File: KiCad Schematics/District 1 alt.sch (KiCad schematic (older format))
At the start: 23 parts

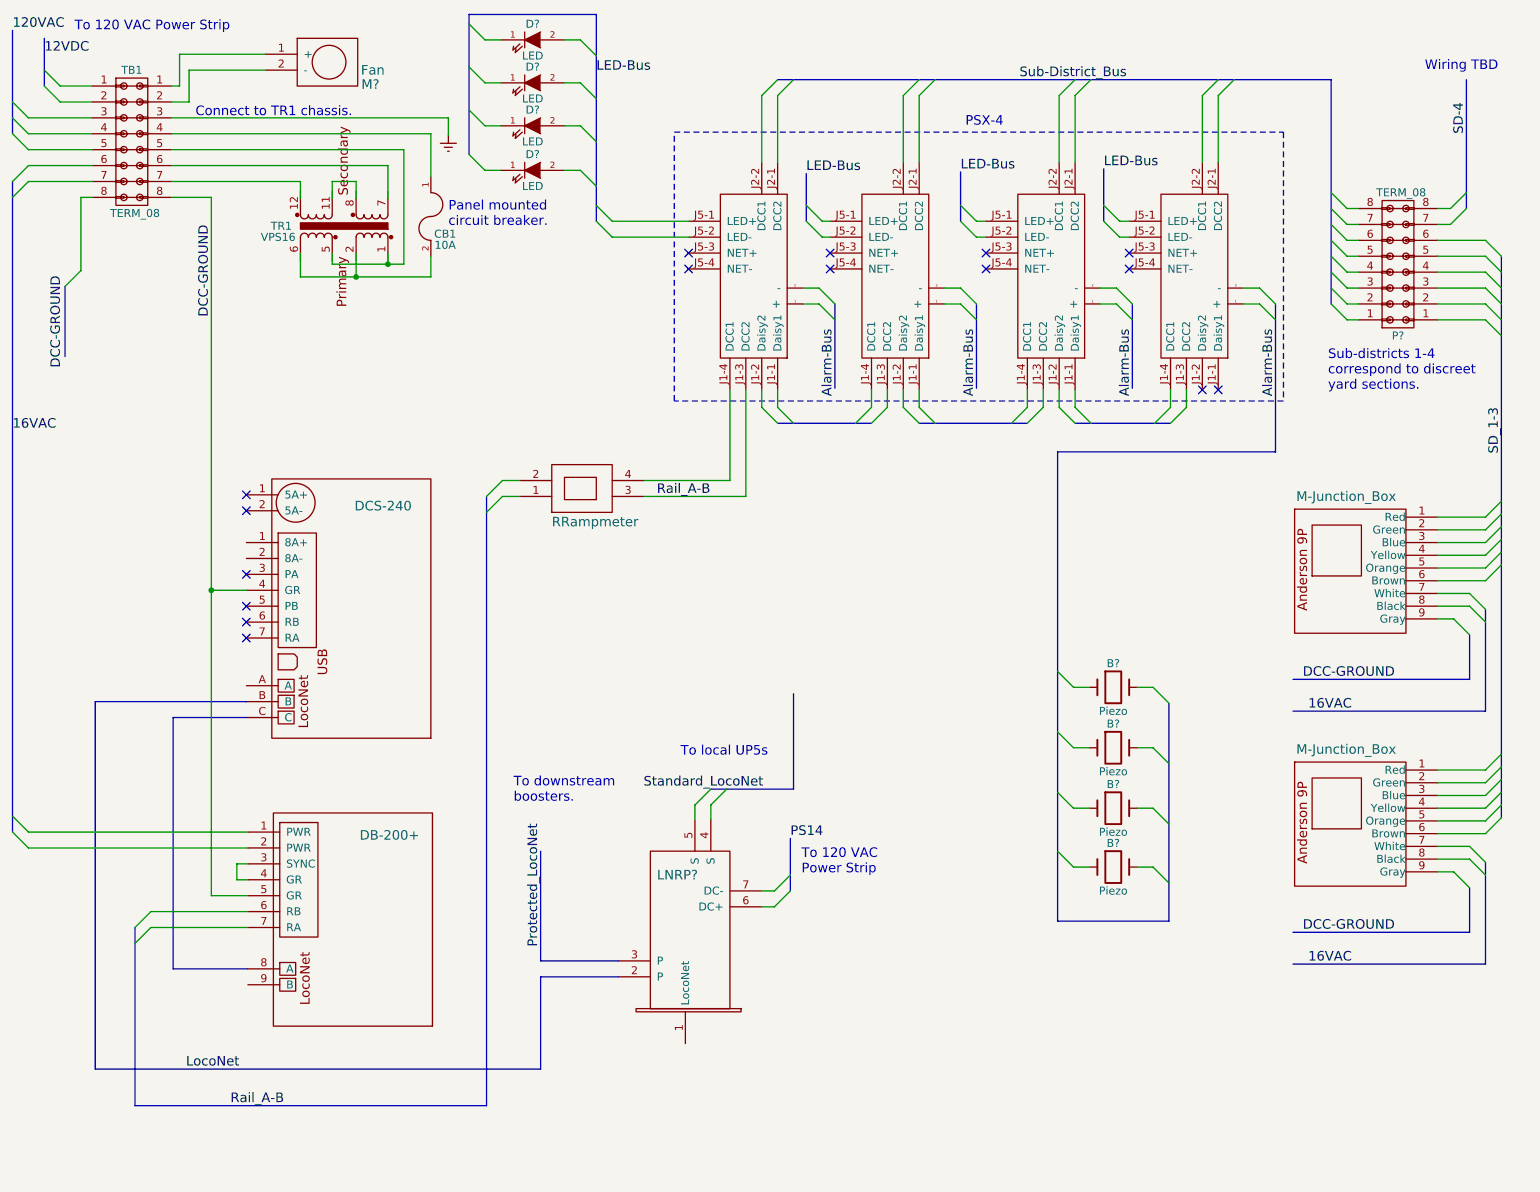
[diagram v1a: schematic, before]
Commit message: Updated schematic to include extra sheets.
Added several alternate wiring sheets and made some changes to the
schematic to reflect team decision. More to come.
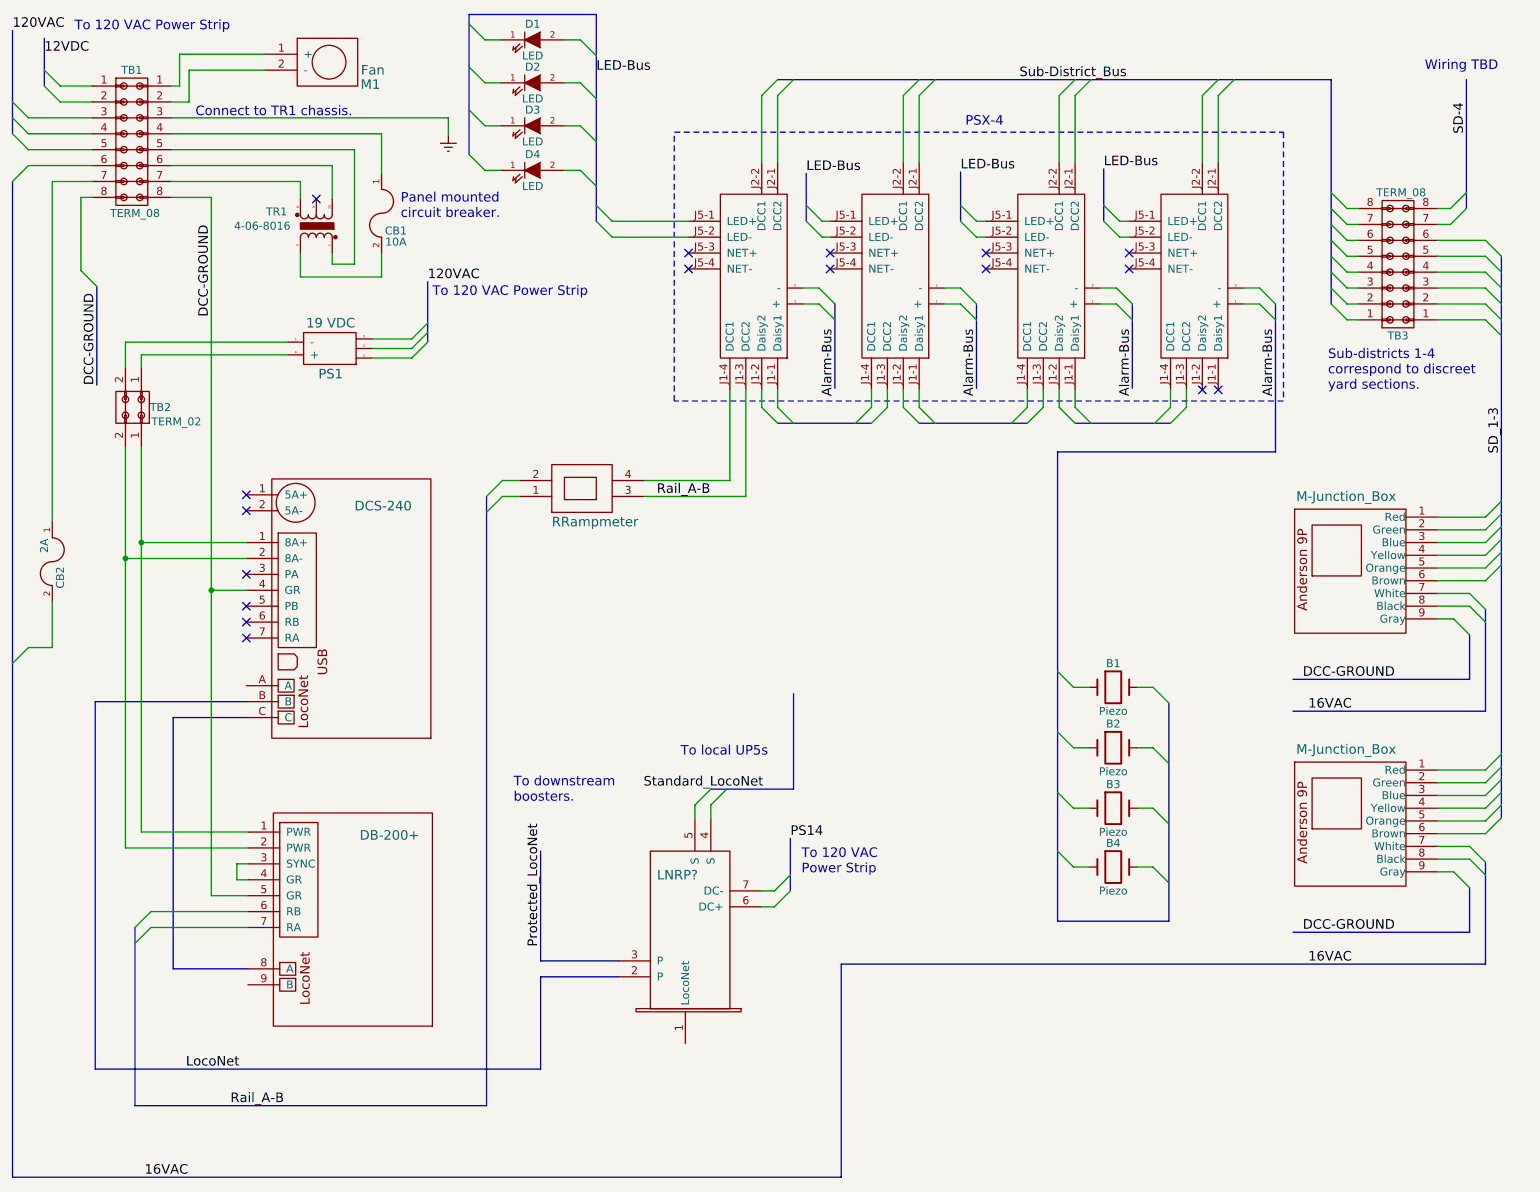
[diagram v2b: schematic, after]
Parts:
- removed TR1: VPS16, symbol TRANSFORMER_VPS16
- added CB2: 2A, symbol FUSE
- added PS1: 19 VDC, symbol AHE220PS19
- added TB2: TERM_02, symbol TERM_02
- added TR1: 4-06-8016, symbol TRANSFORMER_MCI_4-06-8016
- gave numbers to parts that had none: 10
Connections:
- wire segments 142 -> 151
- no-connect marks 16 -> 17
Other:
- moved on the sheet: CB1
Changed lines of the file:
@@
 $Descr USLetter 11000 8500
 encoding utf-8
-Sheet 4 4
+Sheet 4 6
 Title "District 1 Power Box"
-Date "2016-08-27"
-Rev "2"
+Date "2016-09-30"
+Rev "4"
 Comp "North Georgia Modurail"
 Comment1 ""
@@
 120VAC
 $Comp
-L Fan M?
+L Fan M1
 U 1 1 57E26DFA
 P 2340 650
-F 0 "M?" V 2630 1110 60  0000 C CNN
+F 0 "M1" V 2630 1110 60  0000 C CNN
 F 1 "Fan" V 2540 1050 60  0000 L CNN
 F 2 "" H 2340 650 60  0000 C CNN
@@
 	550  1550 650  1450
 Entry Wire Line
-	550  1650 650  1550
-Text Label 550  3120 0    60   ~ 0
+	550  4580 650  4480
+Text Label 1380 7810 0    60   ~ 0
 16VAC
 Text Label 1800 2400 1    60   ~ 0
@@
 $EndComp
 Entry Wire Line
-	550  5640 650  5740
-Entry Wire Line
-	550  5540 650  5640
-Entry Wire Line
 	1320 6240 1420 6140
 Entry Wire Line
@@
 	7230 2970 7330 3070
 $Comp
-L LED D?
+L LED D3
 U 1 1 57E26E02
 P 3820 1200
-F 0 "D?" H 3820 1300 50  0000 C CNN
+F 0 "D3" H 3820 1300 50  0000 C CNN
 F 1 "LED" H 3820 1100 50  0000 C CNN
 F 2 "" H 3820 1200 50  0000 C CNN
@@
 $EndComp
 $Comp
-L LED D?
+L LED D2
 U 1 1 57E26E03
 P 3820 930
-F 0 "D?" H 3820 1030 50  0000 C CNN
+F 0 "D2" H 3820 1030 50  0000 C CNN
 F 1 "LED" H 3820 830 50  0000 C CNN
 F 2 "" H 3820 930 50  0000 C CNN
@@
 $EndComp
 $Comp
-L LED D?
+L LED D4
 U 1 1 57E26E04
 P 3820 1480
-F 0 "D?" H 3820 1580 50  0000 C CNN
+F 0 "D4" H 3820 1580 50  0000 C CNN
 F 1 "LED" H 3820 1380 50  0000 C CNN
 F 2 "" H 3820 1480 50  0000 C CNN
@@
 $EndComp
 $Comp
-L LED D?
+L LED D1
 U 1 1 57E26E05
 P 3820 660
-F 0 "D?" H 3820 760 50  0000 C CNN
+F 0 "D1" H 3820 760 50  0000 C CNN
 F 1 "LED" H 3820 560 50  0000 C CNN
 F 2 "" H 3820 660 50  0000 C CNN
@@
 Standard_LocoNet
 $Comp
-L TERM_08 P?
+L TERM_08 TB3
 U 1 1 57E26E07
 P 9260 2070
-F 0 "P?" H 9260 2520 50  0000 C CNN
+F 0 "TB3" H 9260 2520 50  0000 C CNN
 F 1 "TERM_08" H 9280 1620 50  0000 C CNN
 F 2 "" H 9260 870 50  0000 C CNN
@@
 NoConn ~ 2020 4220
 Entry Wire Line
-	880  2210 980  2110
-Text Label 870  2720 1    60   ~ 0
+	980  2110 1080 2210
+Text Label 1080 2830 1    60   ~ 0
 DCC-GROUND
 $Comp
@@
 	1550 1050 1660 1050
 Wire Wire Line
-	1550 1450 2910 1450
+	1550 1450 2560 1450
 Wire Wire Line
 	1050 1450 650  1450
 Wire Wire Line
-	1050 1550 650  1550
-Wire Wire Line
 	1800 4120 2020 4120
 Wire Wire Line
@@
 Wire Wire Line
 	980  1650 980  2110
-Wire Bus Line
-	550  1550 550  5640
 Wire Wire Line
 	5260 2860 5260 2970
@@
 Wire Wire Line
 	1960 5940 2030 5940
-Wire Wire Line
-	2030 5640 650  5640
-Wire Wire Line
-	2030 5740 650  5740
 Wire Wire Line
 	2030 6140 1420 6140
@@
 	8840 910  8840 2320
 Wire Bus Line
-	880  2210 880  2650
+	1080 2210 1080 2830
 Wire Wire Line
 	9510 1720 9590 1720
@@
 	9690 910  9690 1720
 Wire Wire Line
-	2910 1450 2910 1660
+	2560 1450 2560 1660
 Wire Wire Line
 	2360 2000 2360 2150
 Wire Wire Line
-	2360 2150 3180 2150
-Wire Wire Line
-	1550 1250 3180 1250
-Wire Wire Line
-	1550 1350 3010 1350
+	2360 2150 2870 2150
+Wire Wire Line
+	1550 1250 2870 1250
+Wire Wire Line
+	1550 1350 2700 1350
 Wire Wire Line
 	1550 1150 3290 1150
@@
 	5060 2860 5060 3430
 $Comp
-L Crystal B?
+L Crystal B2
 U 1 1 57E26E09
 P 7470 5110
-F 0 "B?" H 7470 5260 50  0000 C CNN
+F 0 "B2" H 7470 5260 50  0000 C CNN
 F 1 "Piezo" H 7470 4960 50  0000 C CNN
 F 2 "" H 7470 5110 50  0000 C CNN
@@
 $EndComp
 $Comp
-L Crystal B?
+L Crystal B3
 U 1 1 57E26E0A
 P 7470 5490
-F 0 "B?" H 7470 5640 50  0000 C CNN
+F 0 "B3" H 7470 5640 50  0000 C CNN
 F 1 "Piezo" H 7470 5340 50  0000 C CNN
 F 2 "" H 7470 5490 50  0000 C CNN
@@
 $EndComp
 $Comp
-L Crystal B?
+L Crystal B4
 U 1 1 57E26E0B
 P 7470 5860
-F 0 "B?" H 7470 6010 50  0000 C CNN
+F 0 "B4" H 7470 6010 50  0000 C CNN
 F 1 "Piezo" H 7470 5710 50  0000 C CNN
 F 2 "" H 7470 5860 50  0000 C CNN
@@
 $EndComp
 $Comp
-L Crystal B?
+L Crystal B1
 U 1 1 57E26E0C
 P 7470 4730
-F 0 "B?" H 7470 4880 50  0000 C CNN
+F 0 "B1" H 7470 4880 50  0000 C CNN
 F 1 "Piezo" H 7470 4580 50  0000 C CNN
 F 2 "" H 7470 4730 50  0000 C CNN
@@
 L FUSE CB1
 U 1 1 57E26E0E
-P 3180 1770
-F 0 "CB1" V 3290 1860 50  0000 C CNN
-F 1 "10A" V 3360 1860 50  0000 C CNN
-F 2 "" H 3180 1770 50  0000 C CNN
-F 3 "" H 3180 1770 50  0000 C CNN
-	1    3180 1770
+P 2870 1750
+F 0 "CB1" V 2980 1840 50  0000 C CNN
+F 1 "10A" V 3050 1840 50  0000 C CNN
+F 2 "" H 2870 1750 50  0000 C CNN
+F 3 "" H 2870 1750 50  0000 C CNN
+	1    2870 1750
 	0    1    1    0
 $EndComp
 Wire Wire Line
-	3180 2150 3180 2020
-Wire Wire Line
-	3180 1250 3180 1520
-Text Notes 3290 1840 0    60   ~ 0
+	2870 2150 2870 2000
+Wire Wire Line
+	2870 1250 2870 1500
+Text Notes 2990 1790 0    60   ~ 0
 Panel mounted\ncircuit breaker.
 $Comp
@@
 	9710 6270 8600 6270
 Wire Bus Line
-	9810 5830 9810 6470
-Wire Bus Line
-	9810 6470 8600 6470
+	9810 6470 9810 5830
+Wire Bus Line
+	5760 6470 9810 6470
 Wire Bus Line
 	9910 2020 9910 5550
 Text Notes 8820 2870 0    60   ~ 0
 Sub-districts 1-4\ncorrespond to discreet\nyard sections.
-$Comp
-L TRANSFORMER_VPS16 TR1
-U 1 1 57E26E10
-P 2620 1830
-F 0 "TR1" V 2620 2210 50  0000 C CNN
-F 1 "VPS16" V 2550 2230 50  0000 C CNN
-F 2 "" H 2620 1830 60  0000 C CNN
-F 3 "" H 2620 1830 60  0000 C CNN
-	1    2620 1830
+Wire Wire Line
+	2700 1350 2700 2070
+Wire Wire Line
+	2700 2070 2560 2070
+Wire Wire Line
+	2560 2070 2560 2000
+Wire Wire Line
+	1550 1550 2360 1550
+Wire Wire Line
+	2360 1550 2360 1660
+Wire Wire Line
+	1550 1650 1800 1650
+Wire Wire Line
+	1800 1650 1800 6040
+$Comp
+L TRANSFORMER_MCI_4-06-8016 TR1
+U 1 1 57EB2028
+P 2460 1830
+F 0 "TR1" V 2550 2080 50  0000 C CNN
+F 1 "4-06-8016" V 2460 2170 50  0000 C CNN
+F 2 "" H 2460 1670 60  0000 C CNN
+F 3 "" H 2460 1670 60  0000 C CNN
+	1    2460 1830
 	0    -1   -1   0
 $EndComp
-Wire Wire Line
-	2710 2000 2710 2150
-Connection ~ 2710 2150
-Wire Wire Line
-	3010 1350 3010 2070
-Wire Wire Line
-	3010 2070 2560 2070
-Wire Wire Line
-	2560 2070 2560 2000
-Wire Wire Line
-	2910 2000 2910 2070
-Connection ~ 2910 2070
-Wire Wire Line
-	1550 1550 2360 1550
-Wire Wire Line
-	2360 1550 2360 1660
-Wire Wire Line
-	2560 1660 2560 1550
-Wire Wire Line
-	2560 1550 2710 1550
-Wire Wire Line
-	2710 1550 2710 1660
-Wire Wire Line
-	1550 1650 1800 1650
-Wire Wire Line
-	1800 1650 1800 6040
+NoConn ~ 2460 1660
+$Comp
+L AHE220PS19 PS1
+U 1 1 57EB39A2
+P 2550 2600
+F 0 "PS1" H 2550 2760 60  0000 C CNN
+F 1 "19 VDC" H 2550 2440 60  0000 C CNN
+F 2 "" H 2430 2690 60  0000 C CNN
+F 3 "" H 2430 2690 60  0000 C CNN
+	1    2550 2600
+	-1   0    0    1
+$EndComp
+$Comp
+L TERM_02 TB2
+U 1 1 57EB3DDF
+P 1310 2970
+F 0 "TB2" V 1310 3140 50  0000 C CNN
+F 1 "TERM_02" V 1400 3240 50  0000 C CNN
+F 2 "" H 1310 1520 50  0000 C CNN
+F 3 "" H 1310 1520 50  0000 C CNN
+	1    1310 2970
+	0    1    1    0
+$EndComp
+Wire Wire Line
+	2280 2560 1260 2560
+Wire Wire Line
+	1260 2560 1260 2720
+Wire Wire Line
+	2280 2640 1360 2640
+Wire Wire Line
+	1360 2640 1360 2720
+Wire Wire Line
+	1360 3220 1360 5640
+Wire Wire Line
+	1360 3820 2020 3820
+Wire Wire Line
+	2020 3920 1260 3920
+Wire Wire Line
+	1260 3220 1260 5740
+Wire Wire Line
+	1360 5640 2030 5640
+Connection ~ 1360 3820
+Wire Wire Line
+	1260 5740 2030 5740
+Connection ~ 1260 3920
+Wire Wire Line
+	2810 2540 3060 2540
+Wire Wire Line
+	2810 2600 3060 2600
+Wire Wire Line
+	2810 2660 3060 2660
+Entry Wire Line
+	3060 2540 3160 2440
+Entry Wire Line
+	3060 2600 3160 2500
+Entry Wire Line
+	3060 2660 3160 2560
+Wire Bus Line
+	3160 2180 3160 2560
+Text Label 3160 2180 0    60   ~ 0
+120VAC
+Text Notes 3190 2280 0    60   ~ 0
+To 120 VAC Power Strip
+$Comp
+L FUSE CB2
+U 1 1 57EB6162
+P 800 3940
+F 0 "CB2" H 900 3990 50  0000 C CNN
+F 1 "2A" H 700 3890 50  0000 C CNN
+F 2 "" H 800 3940 50  0000 C CNN
+F 3 "" H 800 3940 50  0000 C CNN
+	1    800  3940
+	0    1    1    0
+$EndComp
+Wire Wire Line
+	800  3690 800  1550
+Wire Wire Line
+	800  1550 1050 1550
+Wire Bus Line
+	550  1550 550  7810
+Wire Bus Line
+	550  7810 5760 7810
+Wire Wire Line
+	800  4190 800  4480
+Wire Wire Line
+	800  4480 650  4480
+Wire Bus Line
+	5760 7810 5760 6470
 $EndSCHEMATC

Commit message: Updated schematic
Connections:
- net at DCS?.1 (8A+): now also DB?.1 (PWR), TB2.1 (P1)
- net at DCS?.2 (8A-): now also DB?.2 (PWR), TB2.2 (P2)
- net at TB1.1 (P1): now also M1.1 (+)
- net at TB1.2 (P2): now also M1.2 (-)
- net at TB1.4 (P4): now also CB1.1
- net at TB1.5 (P5): now also TR1.1
- net at TB1.6 (P6): now also TR1.10
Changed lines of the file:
@@
 $Descr USLetter 11000 8500
 encoding utf-8
-Sheet 4 6
+Sheet 4 7
 Title "District 1 Power Box"
 Date "2016-09-30"
